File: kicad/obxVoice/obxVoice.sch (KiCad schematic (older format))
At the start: 45 parts, among them T4 100k, T5 10k

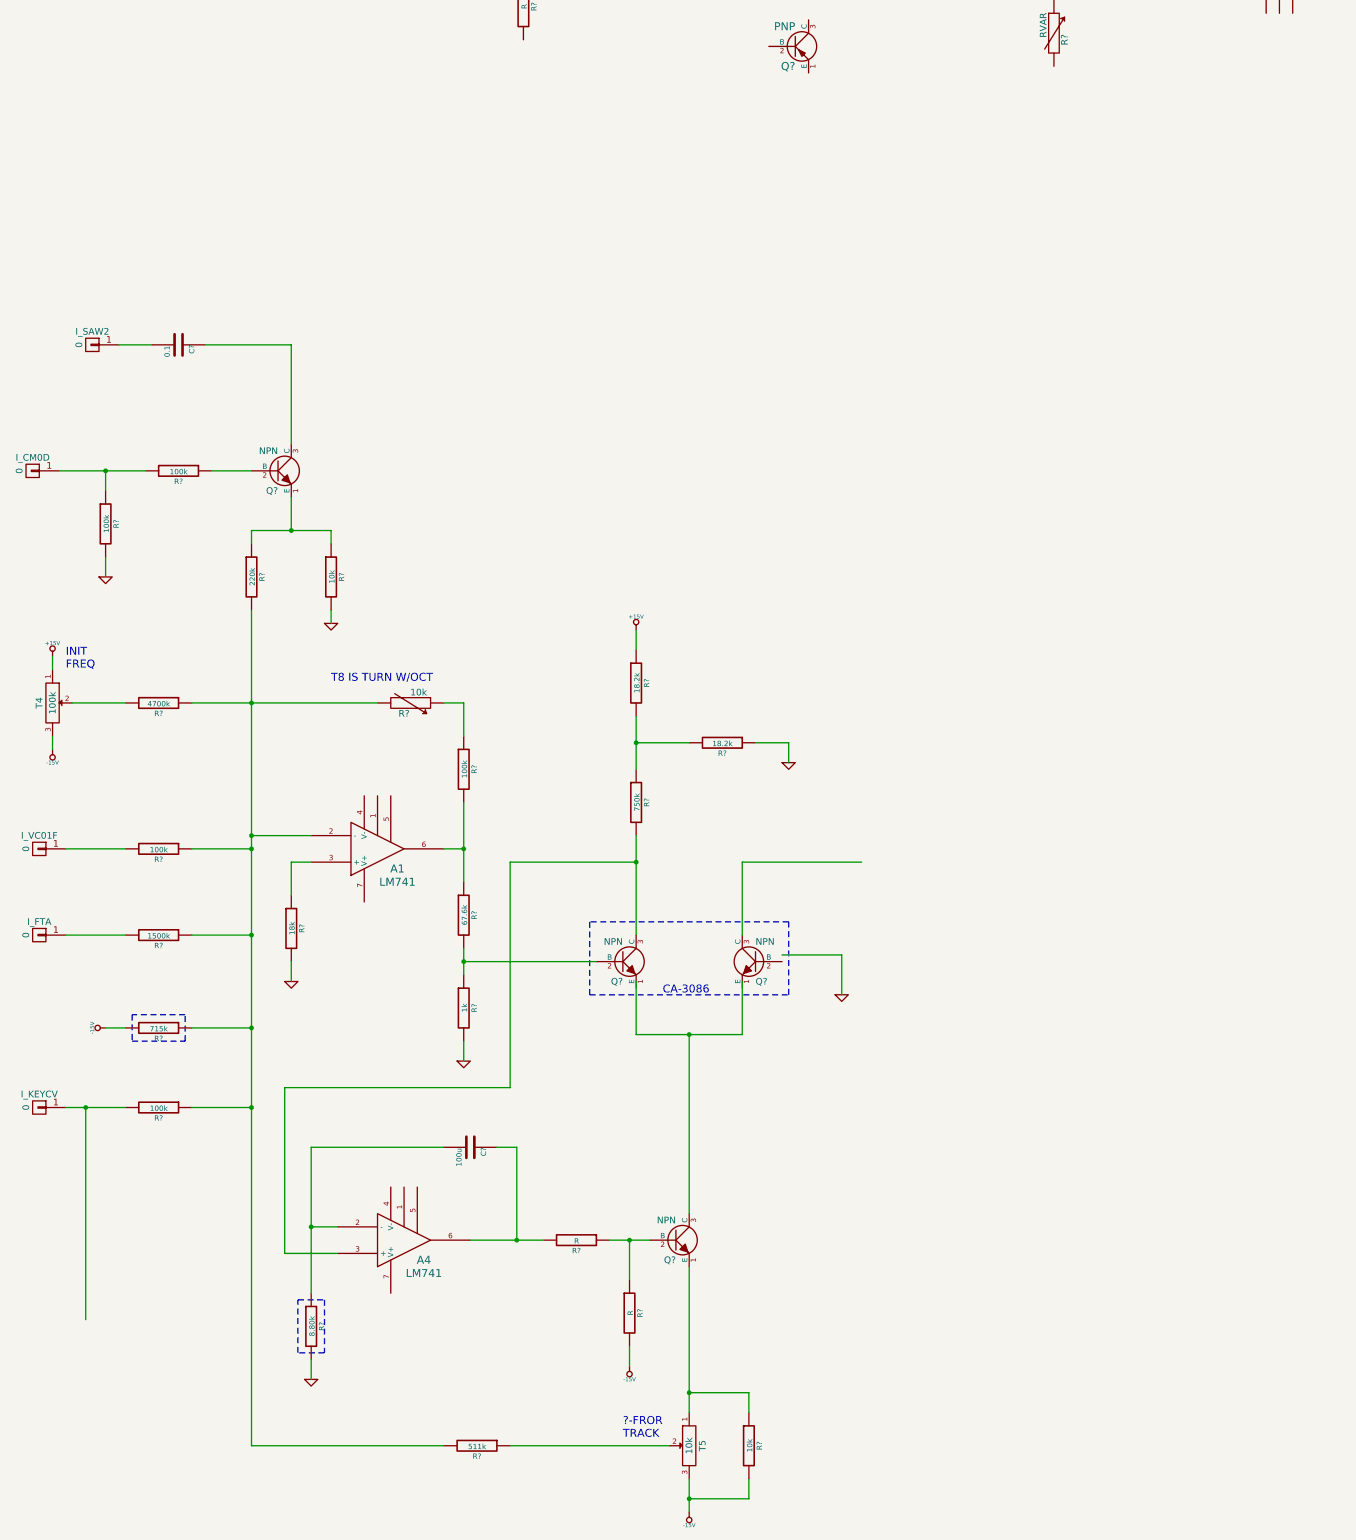
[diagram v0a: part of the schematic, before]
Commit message: Added the +/- 15 volt ports to MAME.lib + a little more work on the OSC1 portion of the OBX schematic.
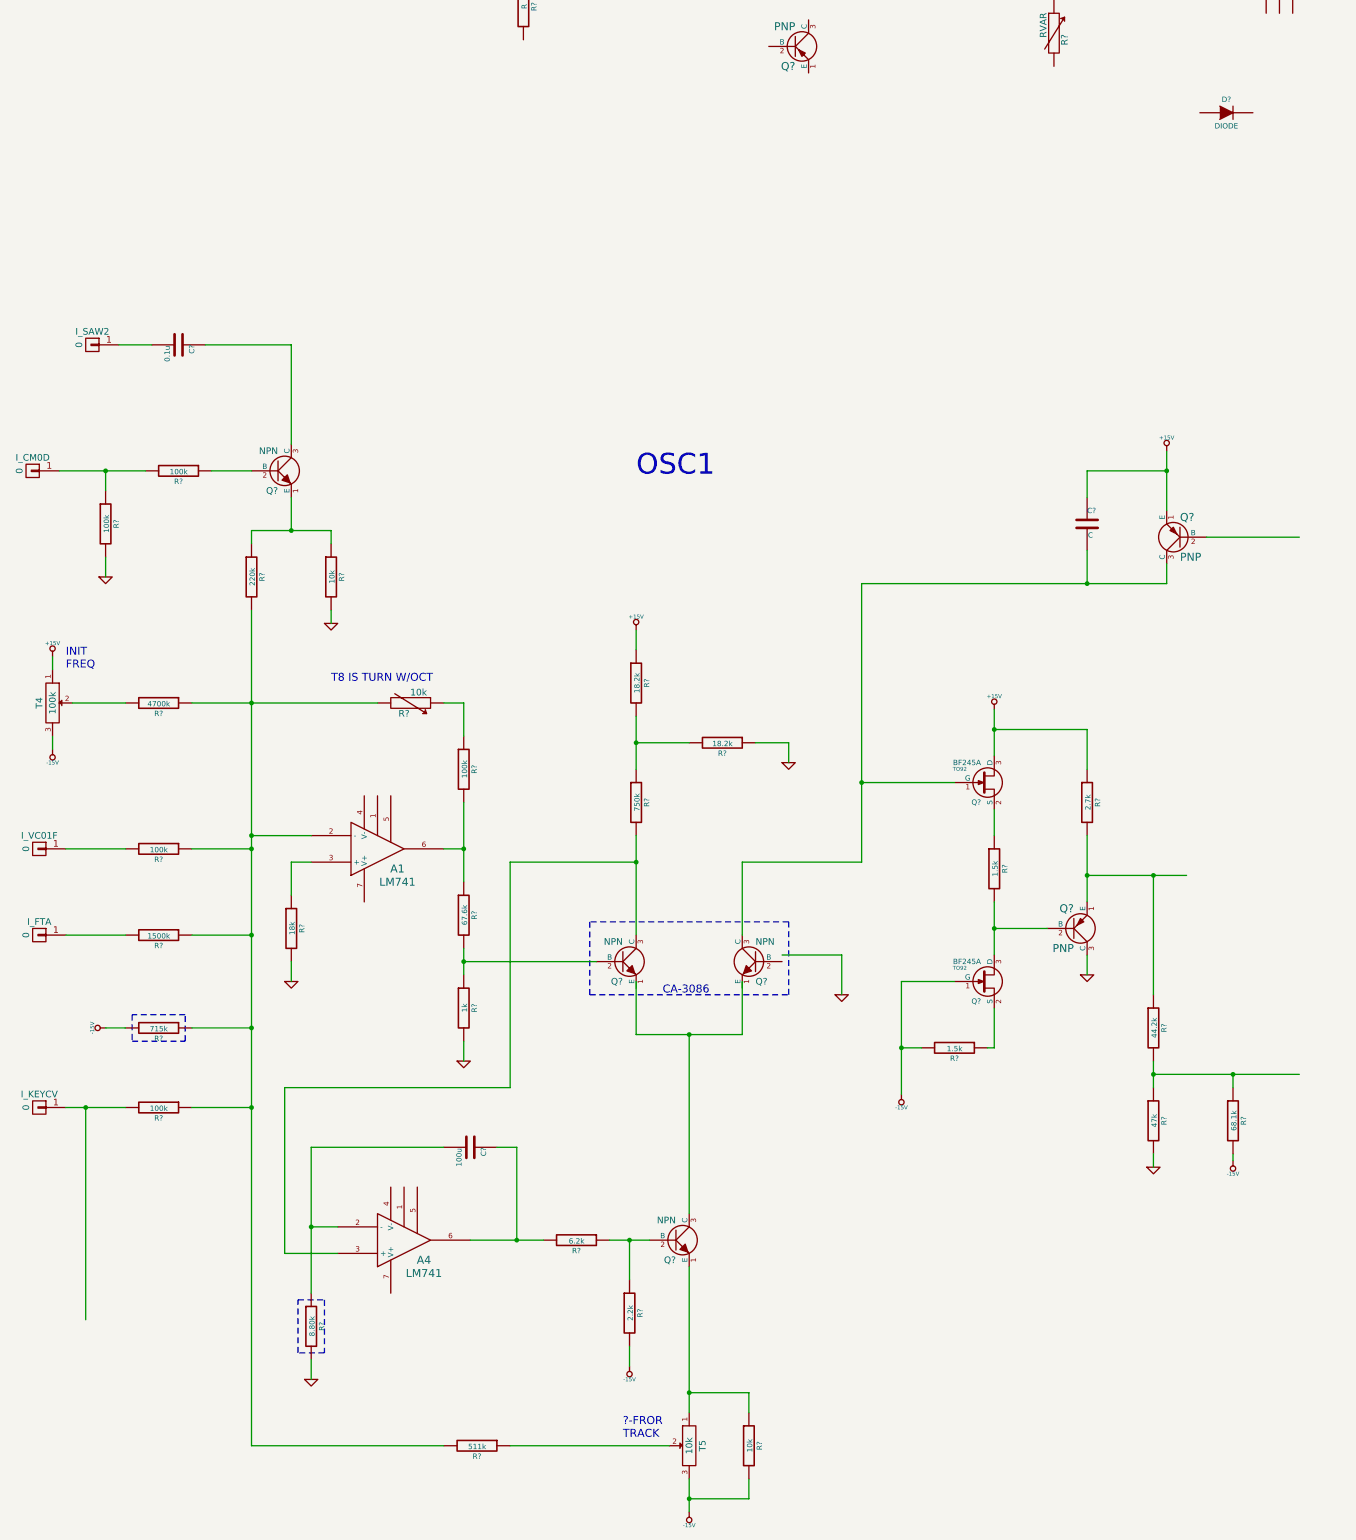
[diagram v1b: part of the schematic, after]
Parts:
- added C?: C, symbol C
- added D?: DIODE, symbol DIODE
- added Q? (x2): BF245A, TO92, symbol BF245A
- added Q? (x2): PNP, symbol PNP
- added R?: 2.7k, symbol R
- added R? (x2): 1.5k, symbol R
- added R?: 44.2k, symbol R
- added R?: 47k, symbol R
- added R?: 68.1k, symbol R
- C?: value 0.1 -> 0.1u
- R?: value R -> 6.2k
- R?: value R -> 2.2k
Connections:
- wire segments 94 -> 103
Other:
- note added: "OSC1"

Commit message: Finished OSC1 for the OBX.
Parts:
- removed C?: C, symbol C
- removed D?: DIODE, symbol DIODE
- removed Q?: NPN, symbol NPN
- removed Q?: PNP, symbol PNP
- removed Q?: BF245A, TO92, symbol BF245A
- removed R?: R, symbol R
- removed R?: RVAR, symbol RVAR
- removed RV?: POT, symbol POT
- removed U?: LM741, symbol LM741
- added A6: TL081, symbol TL081
- added A7: CD4053, symbol CD4053
- added D? (x2): DIODE, symbol DIODE
- added I_PW1, I_SYNC, I_WAVE1: 0, symbol CONN_01X01
- added Q?: PNP, symbol PNP
- added Q? (x3): NPN, symbol NPN
- added R?: 470, symbol R
- added R? (x2): 1k, symbol R
- added R? (x6): 10k, symbol R
- added R?: 55k, symbol R
- added R?: 18.2k, symbol R
- added R?: 28.7k, symbol R
- added R?: 16.2k, symbol R
- added R?: 47k, symbol R
- added R?: 120k, symbol R
- added R? (x2): 22k, symbol R
- added R?: 3.3k, symbol R
- added R?: 4.7k, symbol R
- added R?: 100k, symbol R
- added T6: 10k, symbol POT
- C?: value C -> 1000u
- Q? (x2): value BF245A -> 2N4302; footprint TO92 -> (none)
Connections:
- net labels added: KEYCV
- wire segments 103 -> 223
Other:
- note added: "A3"
- note added: "CA3086"
- note added: "INIT PW"
- note removed: "CA-3086"
- moved on the sheet: R?

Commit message: Oscillator 2 is complete for the OBX now.
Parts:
- added A5, A?: LM741, symbol LM741
- added A8: TL081, symbol TL081
- added A?: CD4053, symbol CD4053
- added C?: 100u, symbol C
- added C?: 1000u, symbol C
- added D?: DIODE, symbol DIODE
- added I_FTB, I_PW2, I_VC02F, I_VC02L, I_WAVE2: 0, symbol CONN_01X01
- added Q? (x7): NPN, symbol NPN
- added Q? (x2): 2N4302, symbol BF245A
- added Q? (x2): PNP, symbol PNP
- added R?: 4700k, symbol R
- added R? (x5): 100k, symbol R
- added R?: 1500k, symbol R
- added R?: 715k, symbol R
- added R?: 18k, symbol R
- added R?: 57.6k, symbol R
- added R? (x2): 1k, symbol R
- added R?: 750k, symbol R
- added R? (x3): 18.2k, symbol R
- added R?: 620k, symbol R
- added R?: 6.2k, symbol R
- added R? (x2): 2.2k, symbol R
- added R?: 511k, symbol R
- added R? (x6): 10k, symbol R
- added R?: 2.7k, symbol R
- added R? (x2): 1.5k, symbol R
- added R?: 44.2k, symbol R
- added R?: 47k, symbol R
- added R?: 68.1k, symbol R
- added R?: 470, symbol R
- added R?: 55k, symbol R
- added R?: 28.7k, symbol R
- added R?: 16.2k, symbol R
- added R?: 120k, symbol R
- added R? (x2): 22k, symbol R
- added R?: 3.3k, symbol R
- added R? (x2): 4.7k, symbol R
- added R?: 12k, symbol R
- added T1: 100k, symbol POT
- added T2, T3: 10k, symbol POT
- added T7: 10k, symbol RVAR
- R?: value 67.6k -> 57.6k
- gave numbers to parts that had none: 1
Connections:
- net +15V: now also C?.1, Q?.1 (E), Q?.3 (D), R?.1, R?.1, R?.1, R?.1, R?.1, R?.2, T1.1
- net -15V: now also Q?.1 (G), R?.1, R?.2, R?.2, R?.2, R?.2, R?.2, R?.2, T1.3, T2.3
- net GND: now also A?.6, A?.8, Q?.1 (E), Q?.1 (E), Q?.1 (E), Q?.1 (E), Q?.2 (B), Q?.3 (C), R?.1, R?.1, R?.2, R?.2, R?.2, R?.2, R?.2, R?.2, T3.3
- net KEYCV: now also R?.2
- net at Q?.1 (E): now also R?.1
- new net: I_VC02F.1 (P1), R?.2
- new net: I_FTB.1 (P1), R?.2
- new net: R?.2, T1.2
- new net: A?.2 (-), R?.1, R?.1, R?.1, R?.1, R?.1, R?.2, T7.2
- new net: A?.3 (+), R?.1
- new net: A?.6, R?.1, R?.2
- new net: R?.1, T7.1
- new net: Q?.2 (B), R?.1, R?.2 (x3)
- new net: C?.2, Q?.1 (G), Q?.3 (C), Q?.3 (C)
- new net: R?.1, R?.2, R?.2
- new net: A5.3 (+), Q?.3 (C), R?.2
- new net: A5.2 (-), C?.2, R?.1
- new net: A5.6, C?.1, R?.2
- new net: Q?.2 (B), R?.1, R?.1
- new net: Q?.1 (E), R?.1, T2.1
- new net: R?.1, T2.2
- new net: Q?.2 (S), R?.1 (x2)
- new net: Q?.2 (B), Q?.3 (D), R?.2
- new net: A8.2 (-), A?.5 (X), R?.1, R?.1, R?.2
- new net: Q?.3 (C), Q?.3 (C), R?.1, R?.2
- new net: Q?.2 (B), Q?.3 (C), R?.2
- new net: D?.1 (A), Q?.2 (B), R?.2
- new net: D?.2 (K), R?.1, R?.1, R?.2
- new net: A8.3 (+), R?.1, R?.1
- new net: A8.6, R?.2
- new net: A?.16, R?.1, R?.2
- new net: A?.3 (Y), R?.1, R?.1
- new net: A?.4, R?.2
- new net: A?.7, R?.1, R?.2
- new net: A?.9, I_WAVE2.1 (P1), R?.2
- new net: R?.2, T3.2
- new net: I_PW2.1 (P1), R?.2
- new net: R?.2, T3.1
- new net: R?.1, R?.1
- new net: I_VC02L.1 (P1), R?.2
- new net: Q?.2 (B), R?.1
- new net: Q?.3 (C), R?.2
- new net SAW2: Q?.1 (E), R?.1, R?.2, R?.2
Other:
- note added: "OSC2"
- note added: "T7 IS TURN W/OCT"

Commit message: Finished the Filter portion of the OBX.
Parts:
- added A10, A12, A14: LM3080, symbol LM3080
- added A11: TL082, symbol TL082
- added A9: TL081, symbol TL081
- added C?: 10u, symbol C
- added C? (x2): 330u, symbol C
- added C?: 0.1u, symbol C
- added D? (x2): DIODE, symbol DIODE
- added I_NOISE, I_RES: 0, symbol CONN_01X01
- added Q?: PNP, symbol PNP
- added R?: 82k, symbol R
- added R? (x2): 68k, symbol R
- added R? (x6): 100k, symbol R
- added R? (x3): 220, symbol R
- added R? (x4): 10k, symbol R
- added R?: 33k, symbol R
- added R?: 47k, symbol R
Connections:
- net GND: now also A10.2, A12.2, A14.2, A9.3 (+), C?.2, C?.2, Q?.2 (B), R?.2, R?.2, R?.2, R?.2
- net at A7.15: now also R?.2
- net at R?.1, R?.1: now also R?.2
- new net: A9.2 (-), C?.2, C?.2, R?.1, R?.1, R?.1, R?.2, R?.2
- new net: A11.1, A11.2 (-), C?.1, R?.1
- new net: A10.3, R?.1, R?.1
- new net: A9.6, R?.1, R?.2
- new net: I_NOISE.1 (P1), R?.2
- new net: A10.5, R?.1
- new net: A10.6, A11.5 (+), C?.1
- new net: R?.2, R?.2
- new net: A11.6 (-), A11.7, R?.1, R?.1, R?.2
- new net: A12.3, R?.1, R?.1
- new net: A12.5, R?.1
- new net: A11.3 (+), A12.6, C?.1
- new net: C?.1, R?.2, R?.2
- new net: D?.1 (A), D?.2 (K), R?.1
- new net: D?.1 (A), D?.2 (K), R?.1, R?.2
- new net: A14.6, R?.1
- new net: A14.3, R?.1, R?.2
- new net: A14.5, Q?.3 (C)
- new net: Q?.1 (E), R?.1
- new net: I_RES.1 (P1), R?.2

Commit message: Finished the VCA section of the OBX.
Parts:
- added A13: LM3080, symbol LM3080
- added A17: TL081, symbol TL081
- added C?: 0.1u, symbol C
- added C?: 100u, symbol C
- added C?: 6.8u, symbol C
- added O_AUDIO: 0, symbol CONN_01X01
- added Q?: PNP, symbol PNP
- added R? (x2): 100k, symbol R
- added R?: 220, symbol R
- added R?: 1000k, symbol R
- added R?: 22k, symbol R
- added R?: 1k, symbol R
- added T11: 100k, symbol POT
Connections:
- net +15V: now also T11.1
- net -15V: now also T11.3
- net GND: now also A13.2, A17.3 (+), Q?.2 (B), R?.2
- net at A11.1, A11.2 (-), C?.1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: now also C?.2
- new net: C?.1, R?.2 (x2)
- new net: A13.3, R?.1, R?.1, R?.1
- new net: A13.5, Q?.3 (C)
- new net: A13.6, A17.2 (-), C?.2, R?.2
- new net: R?.2, T11.2
- new net: Q?.1 (E), R?.1
- new net: A17.6, C?.1, C?.2, R?.1
- new net: O_AUDIO.1 (P1), R?.1
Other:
- note added: "AMPLIFIER\nENVELOPE"
- note added: "FILTER"
- note added: "VCA"
- note added: "VCA\nOFFSET"
